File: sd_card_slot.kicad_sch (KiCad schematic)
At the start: 1 part, among them U17 USB2244I-AEZG-06-TR

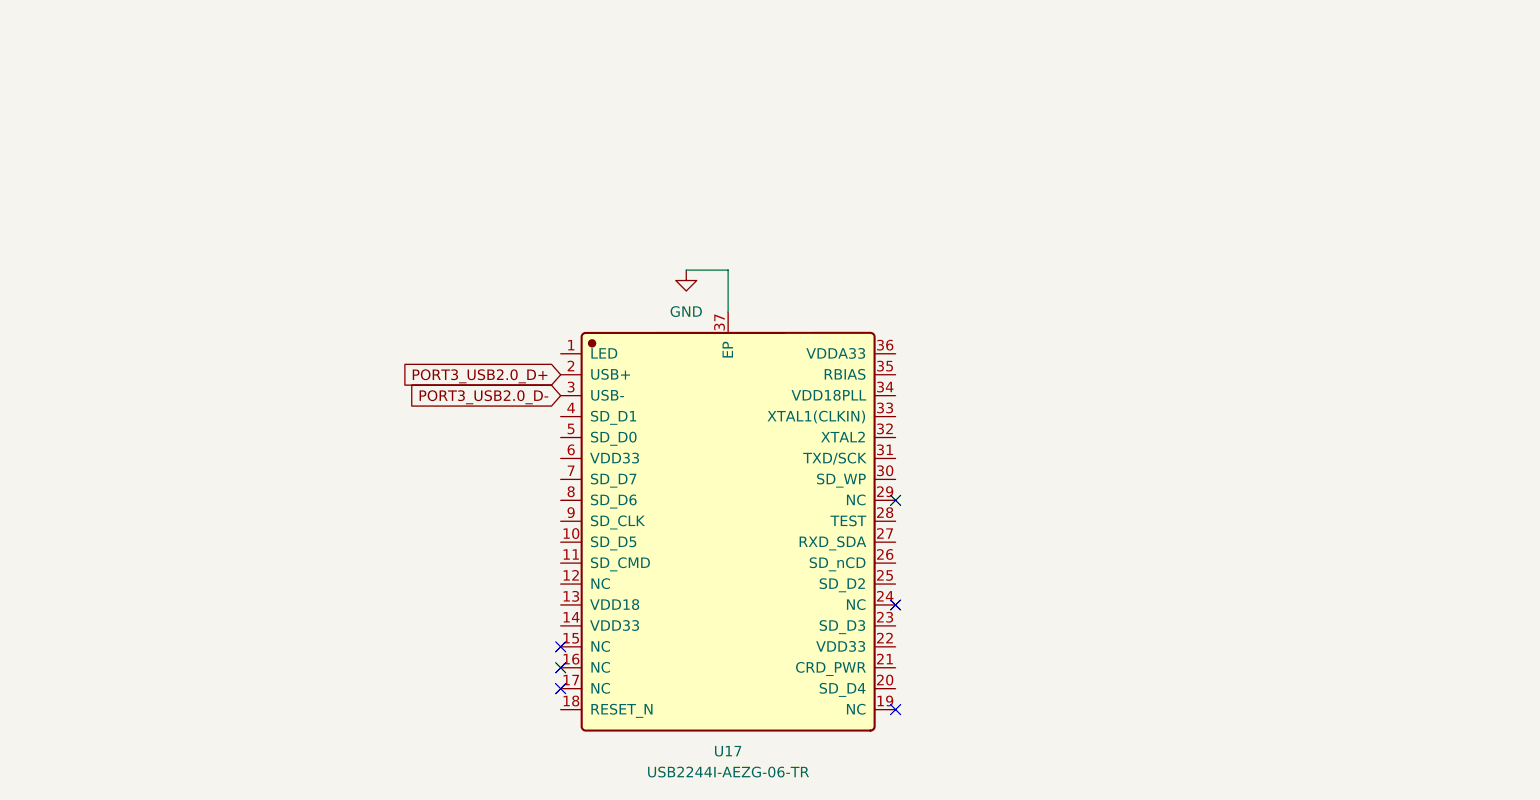
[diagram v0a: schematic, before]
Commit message: Preliminary design of USB2244i USB2.0 -> SD converter
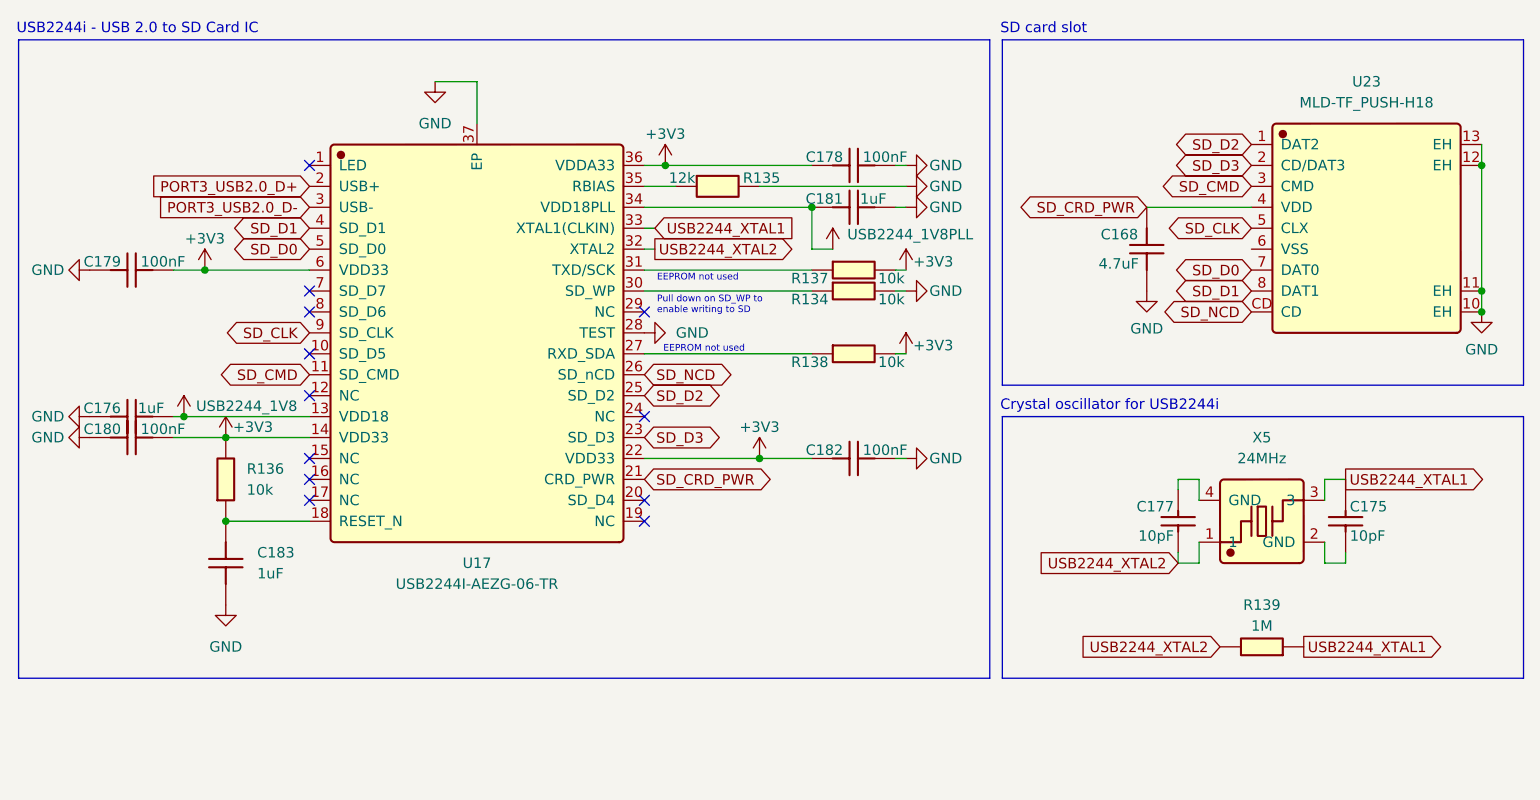
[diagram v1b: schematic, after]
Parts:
- added C168: 4.7uF, Capacitor_SMD:C_0402_1005Metric, symbol JLCImport:CL05A475MP5NRNC
- added C175, C177: 10pF, Capacitor_SMD:C_0603_1608Metric, symbol JLCImport:CL10C100JB8NNNC
- added C176, C181, C183: 1uF, Capacitor_SMD:C_0402_1005Metric, symbol JLCImport:CL05A105KA5NQNC
- added C178, C179, C180, C182: 100nF, Capacitor_SMD:C_0402_1005Metric, symbol JLCImport:CL05B104KB54PNC
- added R134, R136, R137, R138: 10k, Resistor_SMD:R_0402_1005Metric, symbol JLCImport:0402WGF1002TCE
- added R135: 12k, Resistor_SMD:R_0402_1005Metric, symbol JLCImport:CR0402F12K0Q10Z
- added R139: 1M, Resistor_SMD:R_0402_1005Metric, symbol JLCImport:0402WGF1004TCE
- added U23: MLD-TF_PUSH-H18, JLCImport:MLD-TF_PUSH-H18, symbol JLCImport:MLD-TF_PUSH-H18
- added X5: 24MHz, JLCImport:XTM32024000DT00351001, symbol JLCImport:XTM32024000DT00351001
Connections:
- net GND: now also U17.28 (TEST), C168.1, C176.2, C178.1, C179.2, C180.2, C181.1, C182.1, C183.1, R134.2, R135.2, U23.10 (EH), U23.11 (EH), U23.12 (EH), U23.13 (EH)
- net SD_CMD: now reaches U17.11 (SD_CMD)
- net SD_CMD: now also U23.3 (CMD)
- net USB2244_1V8: now reaches U17.13 (VDD18)
- net USB2244_1V8: now also C176.1
- net +3V3: now reaches U17.14 (VDD33)
- net +3V3: now also U17.22 (VDD33), U17.36 (VDDA33), U17.6 (VDD33), C178.2, C179.1, C180.1, C182.2, R136.2, R137.2, R138.2
- net at U17.18 (RESET_N): now also C183.2, R136.1
- net SD_CRD_PWR: now reaches U17.21 (CRD_PWR)
- net SD_CRD_PWR: now also C168.2, U23.4 (VDD)
- net SD_D3: now reaches U17.23 (SD_D3)
- net SD_D3: now also U23.2 (CD/DAT3)
- net SD_D2: now reaches U17.25 (SD_D2)
- net SD_D2: now also U23.1 (DAT2)
- net SD_NCD: now reaches U17.26 (SD_nCD)
- net SD_NCD: now also U23.CD
- net at U17.27 (RXD_SDA): now also R138.1
- net at U17.30 (SD_WP): now also R134.1
- net at U17.31 (TXD/SCK): now also R137.1
- net USB2244_XTAL2: now reaches U17.32 (XTAL2)
- net USB2244_XTAL2: now also C177.2, R139.2, X5.1
- net USB2244_XTAL1: now reaches U17.33 (XTAL1(CLKIN))
- net USB2244_XTAL1: now also C175.2, R139.1, X5.3
- net USB2244_1V8PLL: now reaches U17.34 (VDD18PLL)
- net USB2244_1V8PLL: now also C181.2
- net at U17.35 (RBIAS): now also R135.1
- net SD_D1: now reaches U17.4 (SD_D1)
- net SD_D1: now also U23.8 (DAT1)
- net SD_D0: now reaches U17.5 (SD_D0)
- net SD_D0: now also U23.7 (DAT0)
- net SD_CLK: now reaches U17.9 (SD_CLK)
- net SD_CLK: now also U23.5 (CLX)
- new net: C177.1, X5.4 (GND)
- new net: C175.1, X5.2 (GND)
- no-connect marks 6 -> 12
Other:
- note added: "Crystal oscillator for USB2244i"
- note added: "EEPROM not used"
- note added: "Pull down on SD_WP to enable writing to SD"
- note added: "SD card slot"
- note added: "USB2244i - USB 2.0 to SD Card IC"
- company: (none) -> Designed by: Matthew Kong
- title: (none) -> USB2244i - USB 2.0 to SD card
- moved on the sheet: U17

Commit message: Preliminary design of power monitor for PSU rails and USB-C VBUS
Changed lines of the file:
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@@
+	(wire
+		(pts
+			(xy 91.44 71.12) (xy 90.17 71.12)
+		)
+		(stroke
+			(width 0)
+			(type default)
+		)
+	)
 	(wire
 		(pts
@@
 	)
 	(global_label "SD_CRD_PWR"
-		(shape bidirectional)
+		(shape input)
 		(at 151.13 38.1 180)
 		(fields_autoplaced yes)
@@
 		)
 		(property "Intersheetrefs" "${INTERSHEET_REFS}"
-			(at 134.8174 38.1 0)
+			(at 135.9287 38.1 0)
 			(hide yes)
 			(show_name no)
@@
 	)
 	(global_label "SD_CRD_PWR"
-		(shape bidirectional)
-		(at 90.17 71.12 0)
+		(shape output)
+		(at 91.44 71.12 0)
 		(fields_autoplaced yes)
 		(effects
@@
 		)
 		(property "Intersheetrefs" "${INTERSHEET_REFS}"
-			(at 106.4826 71.12 0)
-			(hide yes)
-			(show_name no)
+			(at 106.6413 71.12 0)
+			(hide yes)
+			(show_name no)

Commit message: Preliminary design of power monitor for USB2244i, 2xRTL9210b + SSD, front panel hub, and 4x chassis fans
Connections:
- net +3V3 renamed +3V3_SD
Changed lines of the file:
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@@
 			)
 		)
-		(property "Value" "+3V3"
-			(at 42.672 64.77 0)
+		(property "Value" "+3V3_SD"
+			(at 44.704 64.77 0)
 			(show_name no)
 			(do_not_autoplace no)
@@
 			)
 		)
-		(property "Value" "+3V3"
+		(property "Value" "+3V3_SD"
 			(at 104.14 64.77 0)
 			(show_name no)
@@
 			)
 		)
-		(property "Value" "+3V3"
-			(at 36.83 41.91 0)
+		(property "Value" "+3V3_SD"
+			(at 35.306 41.91 0)
 			(show_name no)
 			(do_not_autoplace no)
@@
 			)
 		)
-		(property "Value" "+3V3"
-			(at 125.222 54.864 0)
+		(property "Value" "+3V3_SD"
+			(at 127.254 54.61 0)
 			(show_name no)
 			(do_not_autoplace no)
@@
 			)
 		)
-		(property "Value" "+3V3"
+		(property "Value" "+3V3_SD"
 			(at 92.71 29.21 0)
 			(show_name no)
@@
 			)
 		)
-		(property "Value" "+3V3"
-			(at 125.222 44.704 0)
-			(show_name no)
-			(do_not_autoplace no)
+		(property "Value" "+3V3_SD"
+			(at 127.254 44.45 0)
+			(show_name no)
+			(do_not_autoplace no)

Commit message: Mostly complete initial transfer to hierarchical schematic
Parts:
- removed C168: 4.7uF, Capacitor_SMD:C_0402_1005Metric, symbol JLCImport:CL05A475MP5NRNC
- removed C175, C177: 10pF, Capacitor_SMD:C_0603_1608Metric, symbol JLCImport:CL10C100JB8NNNC
- removed C176, C181, C183: 1uF, Capacitor_SMD:C_0402_1005Metric, symbol JLCImport:CL05A105KA5NQNC
- removed C178, C179, C180, C182: 100nF, Capacitor_SMD:C_0402_1005Metric, symbol JLCImport:CL05B104KB54PNC
- removed R134, R136, R137, R138: 10k, Resistor_SMD:R_0402_1005Metric, symbol JLCImport:0402WGF1002TCE
- removed R135: 12k, Resistor_SMD:R_0402_1005Metric, symbol JLCImport:CR0402F12K0Q10Z
- removed R139: 1M, Resistor_SMD:R_0402_1005Metric, symbol JLCImport:0402WGF1004TCE
- removed U17: USB2244I-AEZG-06-TR, JLCImport:USB2244I-AEZG-06-TR, symbol JLCImport:USB2244I-AEZG-06-TR
- removed U23: MLD-TF_PUSH-H18, JLCImport:MLD-TF_PUSH-H18, symbol JLCImport:MLD-TF_PUSH-H18
- removed X5: 24MHz, JLCImport:XTM32024000DT00351001, symbol JLCImport:XTM32024000DT00351001
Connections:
- no-connect marks 12 -> 0
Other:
- note removed: "Crystal oscillator for USB2244i"
- note removed: "EEPROM not used"
- note removed: "Pull down on SD_WP to enable writing to SD"
- note removed: "SD card slot"
- note removed: "USB2244i - USB 2.0 to SD Card IC"
